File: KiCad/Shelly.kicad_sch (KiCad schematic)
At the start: 26 parts, among them J1 Shelly 1, J2 Other, J3 USB-C, Q1 PMF170XP,115, Q2 PMF250XNEX, U1 FT231XQ, U2 LMR16006+FB

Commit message: Library update
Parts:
- J3: footprint RevK:USC16-TR-Round -> RevK:USC16-TR
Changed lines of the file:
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@@
     (property "Reference" "J3" (id 0) (at 156.21 27.94 0))
     (property "Value" "USB-C" (id 1) (at 162.56 35.56 0))
-    (property "Footprint" "RevK:USC16-TR-Round" (id 2) (at 165.1 27.94 0)
+    (property "Footprint" "RevK:USC16-TR" (id 2) (at 165.1 27.94 0)
       (effects (font (size 1.27 1.27)) hide)
     )
@@
     (pin "2")
     (pin "6")
+    (pin "3")
+    (pin "4")
+    (pin "5")
   )
   (symbol (lib_id "Diode:BAV99S") (at 78.74 117.475 0) (unit 2)
@@
       (effects (font (size 1.27 1.27)) hide)
     )
+    (pin "1")
+    (pin "2")
+    (pin "6")
     (pin "3")
     (pin "4")
@@
     (pin "2")
     (pin "6")
+    (pin "3")
+    (pin "4")
+    (pin "5")
   )
   (symbol (lib_id "power:+3.3V") (at 86.36 98.425 270) (unit 1)
@@
       (effects (font (size 1.27 1.27)) hide)
     )
+    (pin "1")
+    (pin "2")
+    (pin "6")
     (pin "3")
     (pin "4")
@@
     )
     (path "/00000000-0000-0000-0000-000060436927"
-      (reference "J3") (unit 1) (value "USB-C") (footprint "RevK:USC16-TR-Round")
+      (reference "J3") (unit 1) (value "USB-C") (footprint "RevK:USC16-TR")
     )
     (path "/00000000-0000-0000-0000-0000610fe01a"

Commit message: Library update
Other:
- note added: "Configure FTDI - Inverted RTS - CBUS0 mode 9"
- note removed: "Configure FTDI for inverted RTS"
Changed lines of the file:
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@@
     (stroke (width 0) (type default) (color 0 0 0 0))
   )
-  (text "Configure FTDI for inverted RTS" (at 175.26 87.63 0)
+  (text "Configure FTDI\n- Inverted RTS\n- CBUS0 mode 9" (at 175.26 87.63 0)
     (effects (font (size 1.27 1.27)) (justify left bottom))
   )

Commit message: Library update
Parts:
- C2: value 0.1uF -> 100nF; footprint RevK:Hidden -> RevK:C_0603_
- C3, C4: footprint RevK:Hidden -> RevK:C_0805_
- D4: footprint RevK:Hidden -> RevK:D_1206_
- L1: footprint RevK:Hidden -> RevK:L_4x4_
- U2: footprint RevK:RegulatorBlockFB -> RevK:SOT-23-Thin-6-Reg
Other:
- moved on the sheet: C1, C5, D3, J3, R1, R2, R3, R4, R5, R6, R7, U1

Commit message: Value
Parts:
- U2: value LMR16006+FB -> LMR16006X; Part No LMR16006YQ3 -> LMR16006X
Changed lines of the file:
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@@
       (effects (font (size 1.27 1.27)) (justify left))
     )
-    (property "Value" "LMR16006+FB" (id 1) (at 248.285 91.2372 0)
+    (property "Value" "LMR16006X" (id 1) (at 248.285 91.2372 0)
       (effects (font (size 1.27 1.27)) (justify left))
     )
@@
       (effects (font (size 1.27 1.27)) hide)
     )
-    (property "Part No" "LMR16006YQ3" (id 5) (at 214.63 84.455 0)
+    (property "Part No" "LMR16006X" (id 5) (at 214.63 84.455 0)
       (effects (font (size 1.27 1.27)) hide)
     )
@@
     )
     (path "/f55b8cc2-ae03-479b-8077-c44111b7cc43"
-      (reference "U2") (unit 1) (value "LMR16006+FB") (footprint "RevK:SOT-23-Thin-6-Reg")
+      (reference "U2") (unit 1) (value "LMR16006X") (footprint "RevK:SOT-23-Thin-6-Reg")
     )
   )

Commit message: Changed to using jlcpcb production plugin
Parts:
- J1, J2: now left out of the parts list
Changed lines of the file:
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@@
   )
   (symbol (lib_id "Connector_Generic:Conn_01x05") (at 73.66 43.18 0) (unit 1)
-    (in_bom yes) (on_board yes)
+    (in_bom no) (on_board yes)
     (property "Reference" "J1" (id 0) (at 72.39 34.29 0)
       (effects (font (size 1.27 1.27)) (justify left))
@@
   )
   (symbol (lib_id "Connector_Generic:Conn_01x06") (at 73.66 69.85 0) (unit 1)
-    (in_bom yes) (on_board yes)
+    (in_bom no) (on_board yes)
     (property "Reference" "J2" (id 0) (at 72.39 60.96 0)
       (effects (font (size 1.27 1.27)) (justify left))

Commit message: Production order
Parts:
- C2: LCSC Part # (none) -> C30926
- C3: LCSC Part # (none) -> C19110
- C4: LCSC Part # (none) -> C17024
- D1, D2: footprint Package_TO_SOT_SMD:SOT-363_SC-70-6 -> RevK:SOT-363_SC-70-6-Rot; LCSC Part # (none) -> C68987
- D3: LCSC Part # (none) -> C264473
- D4: LCSC Part # (none) -> C143805; Part No CD1206-B2100 -> (none)
- J1: footprint Connector_PinHeader_2.54mm:PinHeader_1x05_P2.54mm_Vertical -> RevK:PinHeader_1x05_P2.54mm_Right; LCSC Part # (none) -> C225491; now in the parts list
- J2: footprint Connector_PinHeader_1.27mm:PinHeader_1x06_P1.27mm_Vertical -> RevK:PinHeader_1x06_P1.27mm_Vertical; LCSC Part # (none) -> C2832273; now in the parts list
- J3: LCSC Part # (none) -> C709357; Note Available from Toby Electronics -> (none)
- L1: footprint RevK:L_4x4_ -> RevK:L_1210_; LCSC Part # (none) -> C560045; Manufacturer Laird -> (none); Part No TYA4020 -> (none)
- Q1, Q2: footprint Package_TO_SOT_SMD:SOT-323_SC-70 -> RevK:SOT-323_SC-70
- R6: value 100k 1% or 0R -> 100k 1%; LCSC Part # (none) -> C14675
- R7: value 30k 1% or NF -> 30k 1%; LCSC Part # (none) -> C100001
- U1: footprint RevK:QFN-20-1EP_4x4mm_P0.5mm_EP2.5x2.5mm -> RevK:QFN-20-1EP_4x4mm_P0.5mm_EP2.5x2.5mm-Rot; LCSC Part # (none) -> C132159
- U2: value LMR16006X -> LMR16006XDDCR; footprint RevK:SOT-23-Thin-6-Reg -> RevK:SOT-23-Thin-6-Reg2; LCSC Part # (none) -> C87080; Manufacturer TI -> (none); Part No LMR16006X -> (none)
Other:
- moved on the sheet: C5

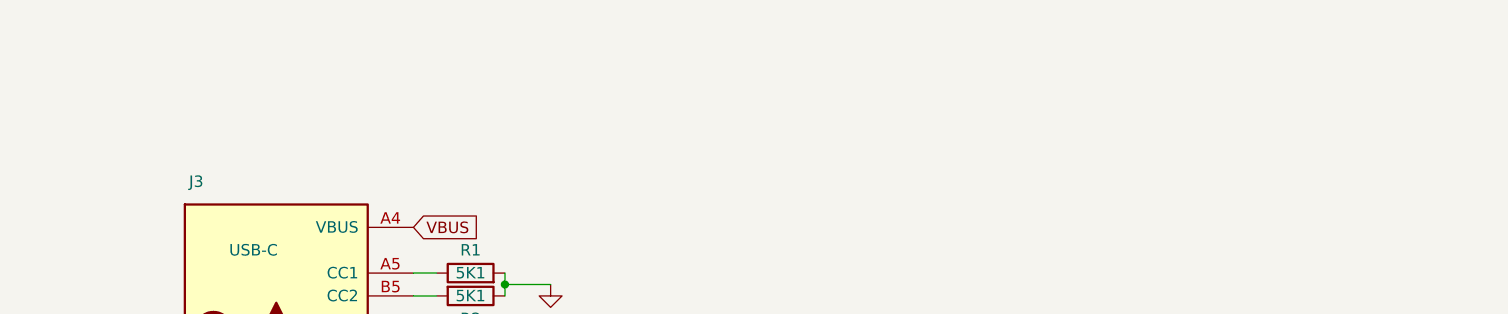
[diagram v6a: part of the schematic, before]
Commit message: Note on more suitable regulator
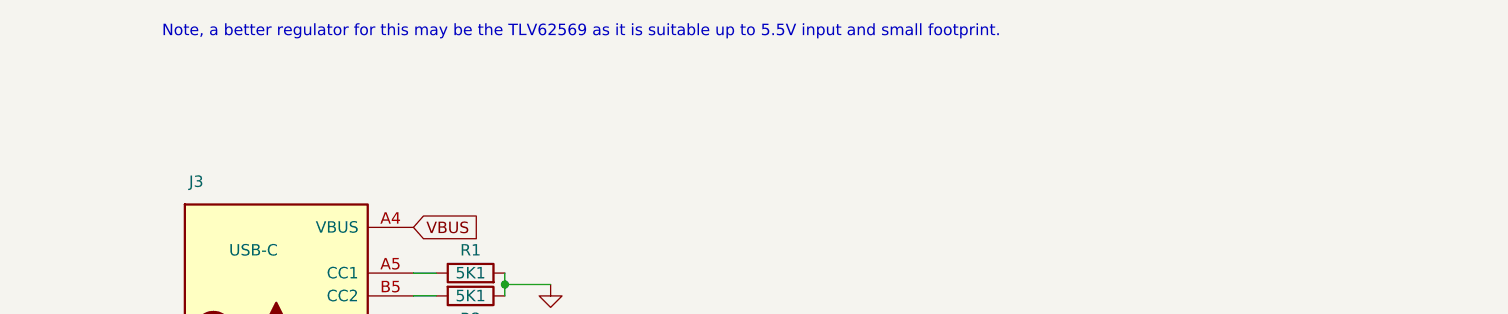
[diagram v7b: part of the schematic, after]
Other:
- note added: "Note, a better regulator for this may be the TLV62569 as it is suitable up to 5.5V input and small footprint."
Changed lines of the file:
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@@
+    (effects (font (size 1.27 1.27)) (justify left bottom))
+  )
+  (text "Note, a better regulator for this may be the TLV62569 as it is suitable up to 5.5V input and small footprint."
+    (at 125.73 24.765 0)
     (effects (font (size 1.27 1.27)) (justify left bottom))
   )
